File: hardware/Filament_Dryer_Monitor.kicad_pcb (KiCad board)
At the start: 4 copper layers, 91 x 52 mm, 109 parts, among them J1 DC Connector, J2 USB_C_Receptacle_USB2.0_16P, J3 Sensor, J4 Display, J5 Heater Connector, J6 Fan Connector, J7 NTC Connector, Q1 NTD20P06LT4G, Q2 MMBT3904, Q3 MMBT3904, Q4 IRLR3636TRPBF, Q5 IRLML2060TRPBF, Q6 MMBT3904, Q7 MMBT3904, U1 TLV1701, U2 CP2102-GM, U3 AKS1201, U4 ESP32-WROOM-32E-N4, U5 L7987L

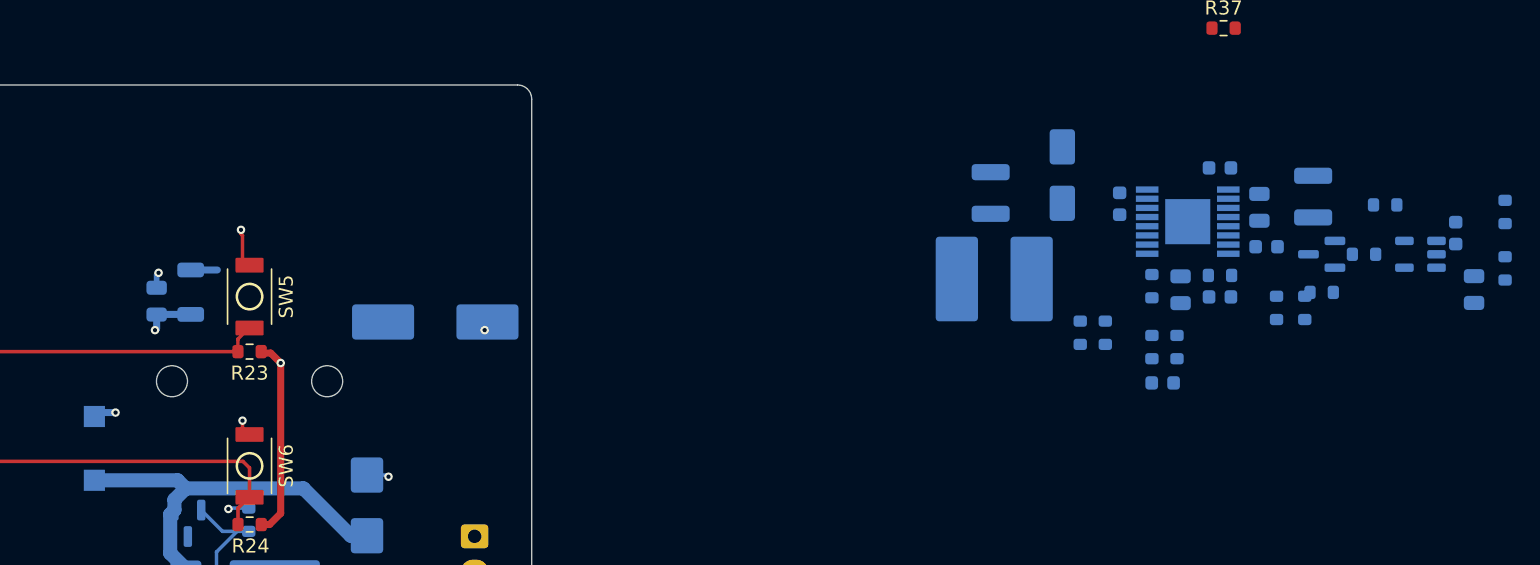
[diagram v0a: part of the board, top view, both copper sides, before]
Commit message: Uopdated buck layout
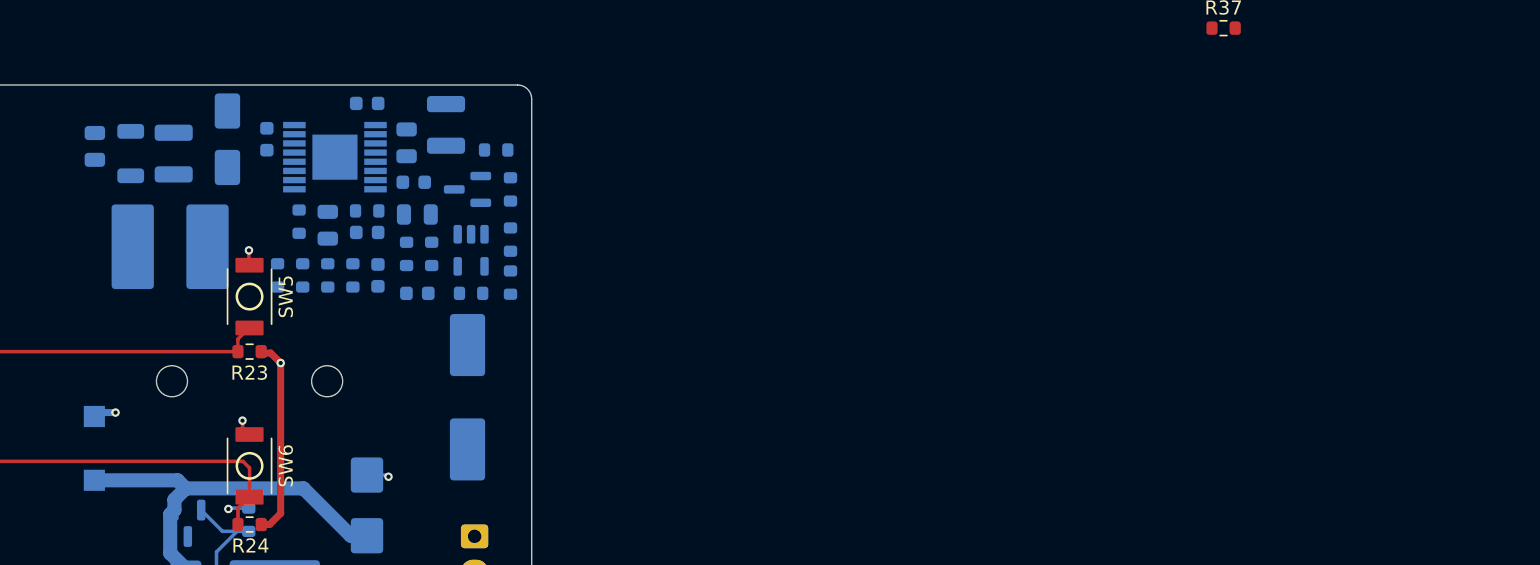
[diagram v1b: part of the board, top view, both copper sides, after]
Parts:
- moved C7 75.1 mm to (182.9, 89.2), turned to 180 degrees
- moved C2 73.7 mm to (182.9, 94.8), turned to 180 degrees
- moved R2 73.3 mm to (186.7, 94.8), turned to 180 degrees
- moved R1 70.7 mm to (189.5, 94.0), turned to -90 degrees
- moved U1 67.3 mm to (186.7, 91.7), turned to -90 degrees
- moved R5 62.1 mm to (189.5, 91.0), turned to 90 degrees
- moved R32 62.0 mm to (183.9, 92.0), turned to -90 degrees
- moved R31 61.8 mm to (182.1, 92.0)
- moved C1 61.7 mm to (184.9, 82.8)
- moved Q7 60.7 mm to (186.4, 87.4)
- moved R6 60.7 mm to (189.5, 87.4), turned to 90 degrees
- moved C4 60.6 mm to (182.6, 86.9)
- moved C21 60.6 mm to (179.3, 81.3)
- moved C3 60.6 mm to (182.1, 84.1)
- moved C6 60.6 mm to (172.2, 83.8)
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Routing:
- net GND: track 55.5 -> 51.1 mm, vias 28 -> 26
- net 3V3_MCU: track 51.5 -> 47.9 mm, vias 13 -> 12
- net Net-(D7-K): track 0.00 -> 1.89 mm
- net /Power/3V3_BUCK: track 1.89 -> 0.00 mm

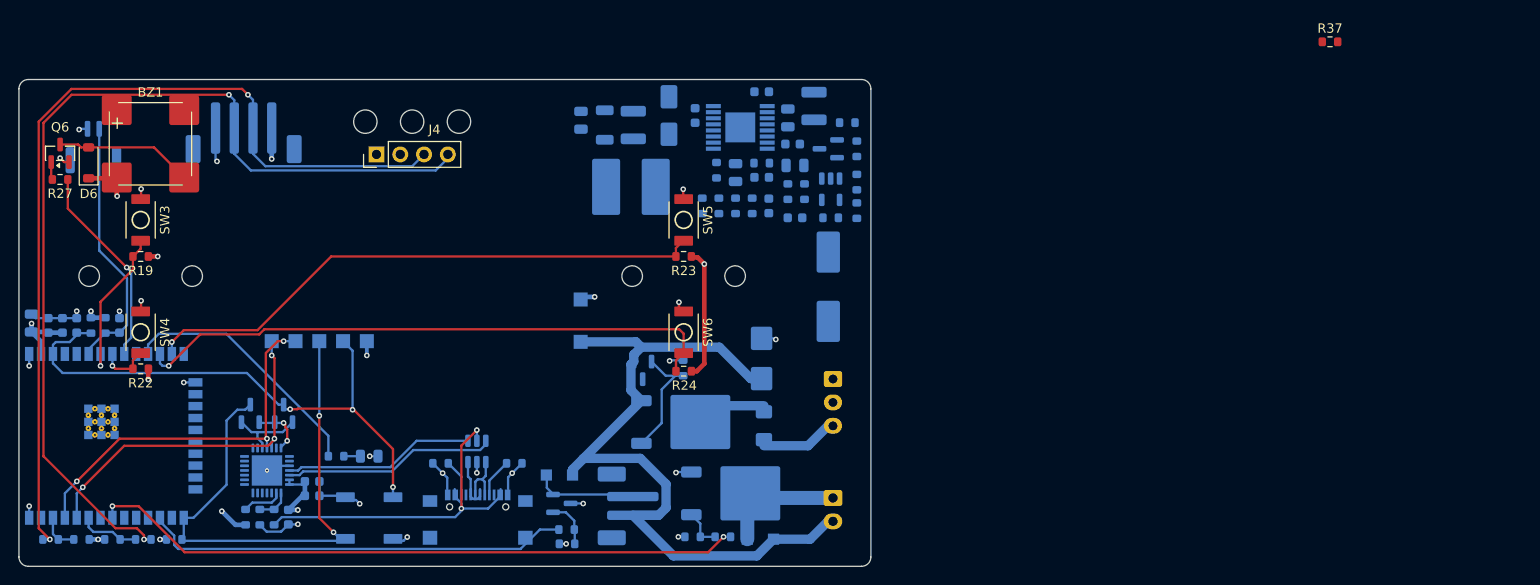
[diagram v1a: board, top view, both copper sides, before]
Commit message: updated layout
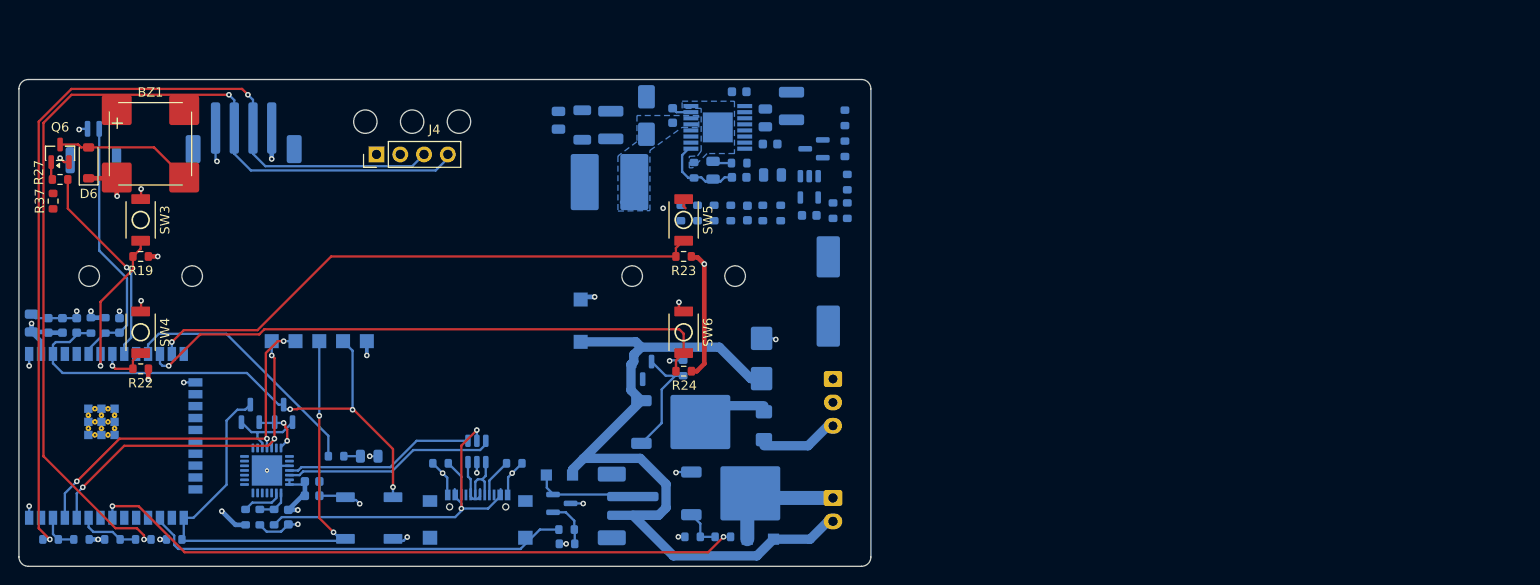
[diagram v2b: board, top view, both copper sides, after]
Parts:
- moved R37 137.5 mm to (103.6, 93.0), turned to 90 degrees
- moved R31 3.52 mm to (179.5, 94.3)
- moved R32 3.42 mm to (181.4, 94.3)
- moved C7 2.61 mm to (180.5, 90.2)
- moved C9 2.42 mm to (174.1, 89.7)
- moved C20 2.41 mm to (177.8, 94.3)
- moved R29 2.41 mm to (170.7, 94.3)
- moved R35 2.41 mm to (176.0, 94.3)
- moved R36 2.41 mm to (174.3, 94.3)
- moved R4 2.41 mm to (172.5, 94.3)
- moved C10 2.40 mm to (163.2, 84.9)
- moved FB1 2.40 mm to (160.2, 84.9)
- moved C1 2.40 mm to (182.5, 82.8)
- moved C11 2.40 mm to (157.6, 84.4)
- moved C21 2.40 mm to (176.9, 81.3)
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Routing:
- net Net-(U5-FB): track 0.00 -> 8.98 mm
- net Net-(U5-BOOT): track 0.00 -> 2.12 mm
- net Net-(C9-Pad1): track 0.00 -> 2.00 mm
- added copper zone on B.Cu, net GND
- added copper zone on B.Cu, net Net-(D7-K)

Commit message: Layout update
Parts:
- turned C1 to 90 degrees
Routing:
- net 3V3_MCU: track 47.9 -> 215.2 mm, vias 12 -> 10
- net 24V_PROT: track 79.7 -> 136.5 mm, vias 0 -> 3
- net /Power/3V3_BUCK: track 0.00 -> 50.3 mm, vias 0 -> 2
- net GND: track 51.1 -> 78.3 mm, vias 26 -> 46
- net /Power/EN: track 0.00 -> 17.6 mm, vias 0 -> 2
- net Net-(D6-A): track 14.7 -> 0.33 mm
- net /Power/COMP: track 0.00 -> 9.65 mm
- net Net-(U5-ILIM): track 0.00 -> 9.01 mm
- net Net-(U5-FSW): track 0.00 -> 8.73 mm
- net /Power/VREF_FAULT: track 0.00 -> 7.88 mm
- net Net-(R5-Pad2): track 0.00 -> 6.15 mm
- net Net-(U5-FB): track 8.98 -> 14.3 mm
- net Net-(Q7-B): track 0.00 -> 4.07 mm
- net Net-(U5-SS): track 0.00 -> 2.27 mm
- net Net-(C20-Pad1): track 0.00 -> 1.80 mm
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- added copper zone on B.Cu, net /Power/3V3_BUCK
- added copper zone on B.Cu, net 24V_PROT
- removed copper zone on In2.Cu, net 3V3_MCU

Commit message: Update Filament_Dryer_Monitor.kicad_pcb
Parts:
- turned D1 to 180 degrees
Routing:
- net GND: track 78.3 -> 83.5 mm, vias 46 -> 47
- net 24V_PROT: track 136.5 -> 139.6 mm

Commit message: Added C22 1uF
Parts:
- moved C5 0.25 mm to (186.2, 102.6)
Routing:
- net 3V3_MCU: track 215.2 -> 231.6 mm
- net Net-(D6-A): track 0.33 -> 9.11 mm
- net 24V_PROT: vias 3 -> 2

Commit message: updated vias on U5 and D7
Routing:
- net GND: vias 47 -> 48
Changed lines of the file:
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@@
+	)
+	(via
+		(at 173.749 87.35)
+		(size 0.6)
+		(drill 0.3)
+		(layers "F.Cu" "B.Cu")
+		(net "GND")
 	)
 	(via
@@
 	(via
 		(at 152.668 129.058)
+		(size 0.6)
+		(drill 0.3)
+		(layers "F.Cu" "B.Cu")
+		(net "GND")
+	)
+	(via
+		(at 173.749 82.9)
 		(size 0.6)
 		(drill 0.3)
@@
 	)
 	(via
+		(at 175.549 82.9)
+		(size 0.6)
+		(drill 0.3)
+		(layers "F.Cu" "B.Cu")
+		(net "GND")
+	)
+	(via
+		(at 175.55 87.35)
+		(size 0.6)
+		(drill 0.3)
+		(layers "F.Cu" "B.Cu")
+		(net "GND")
+	)
+	(via
 		(at 101.092 110.586)
 		(size 0.6)
@@
 	)
 	(via
-		(at 174.649 85.116)
-		(size 0.6)
-		(drill 0.3)
-		(layers "F.Cu" "B.Cu")
-		(net "GND")
-	)
-	(via
-		(at 173.496 86.132)
-		(size 0.6)
-		(drill 0.3)
-		(layers "F.Cu" "B.Cu")
-		(net "GND")
-	)
-	(via
 		(at 170.702 94.335)
 		(size 0.6)
@@
 	)
 	(via
-		(at 175.782 86.132)
-		(size 0.6)
-		(drill 0.3)
-		(layers "F.Cu" "B.Cu")
-		(net "GND")
-	)
-	(via
 		(at 103.646 94.514)
 		(size 0.6)
@@
 	)
 	(via
-		(at 175.782 84.1)
+		(at 174.649 82.9)
+		(size 0.6)
+		(drill 0.3)
+		(layers "F.Cu" "B.Cu")
+		(net "GND")
+	)
+	(via
+		(at 174.65 87.35)
 		(size 0.6)
 		(drill 0.3)
@@
 		(net "GND")
 	)
-	(via
-		(at 173.496 84.1)
-		(size 0.6)
-		(drill 0.3)
-		(layers "F.Cu" "B.Cu")
-		(net "GND")
-	)

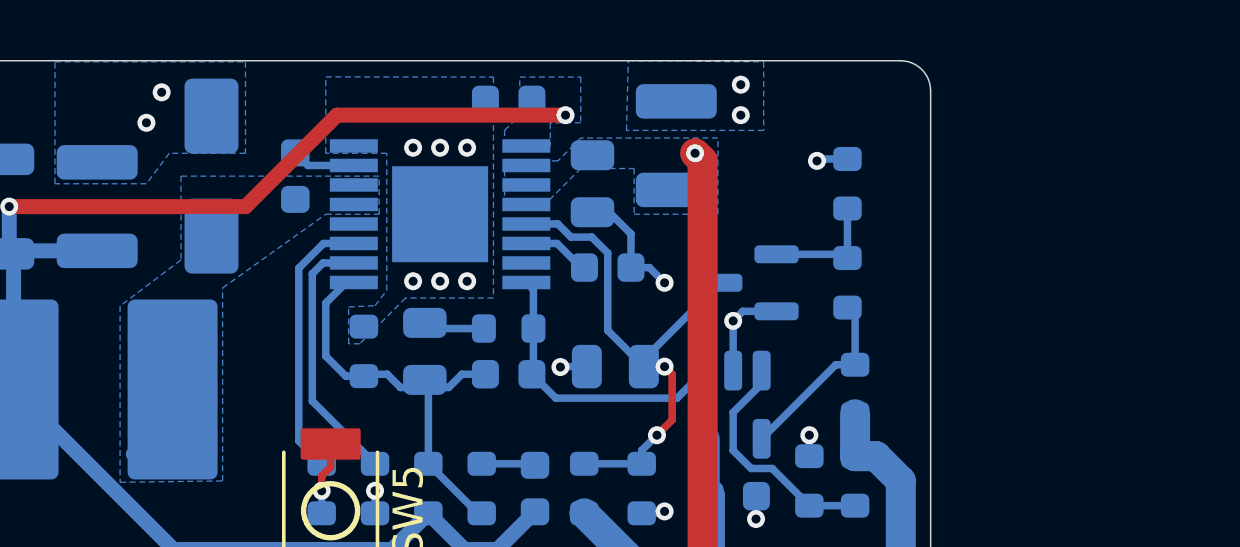
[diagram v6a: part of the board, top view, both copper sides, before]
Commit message: updated D7 footprint
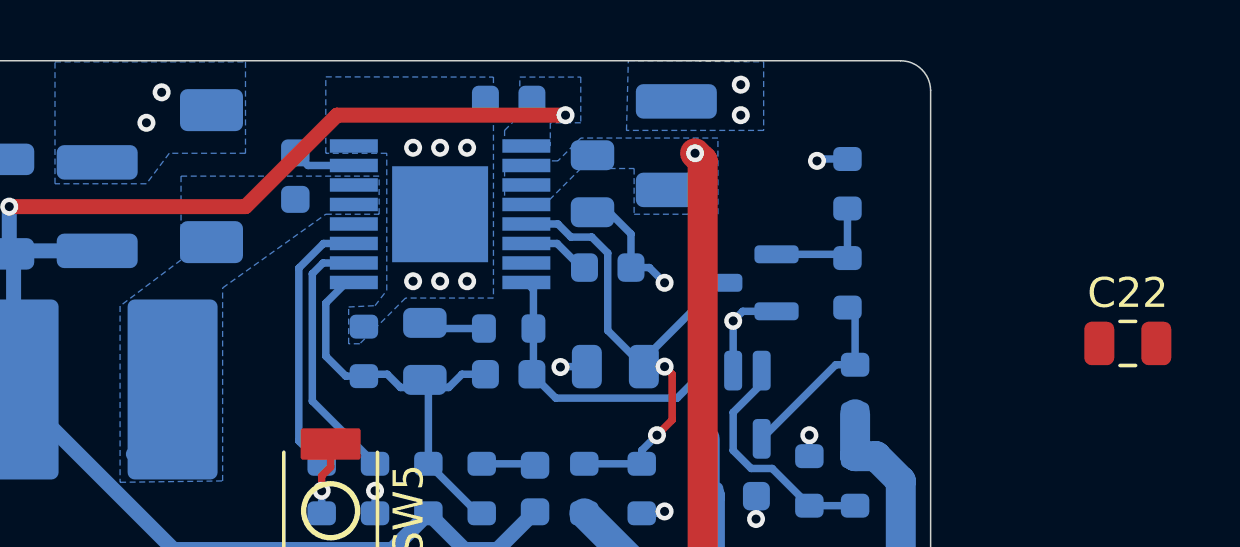
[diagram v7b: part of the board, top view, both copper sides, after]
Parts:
- added C22: 1u, Capacitor_SMD:C_0805_2012Metric, F.Cu at (197.6, 89.4)
- D7: value STPS2L60A -> PMEG6030EP; footprint Diode_SMD:D_SMA -> Diode_SMD:D_SOD-128

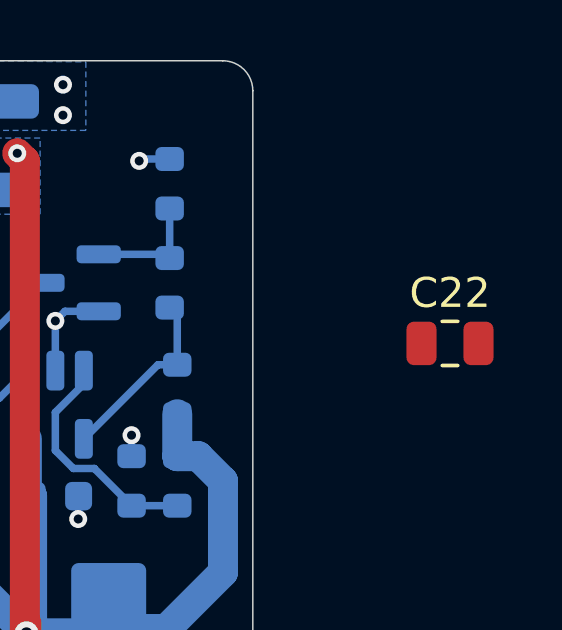
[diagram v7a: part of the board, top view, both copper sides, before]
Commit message: Removed C22
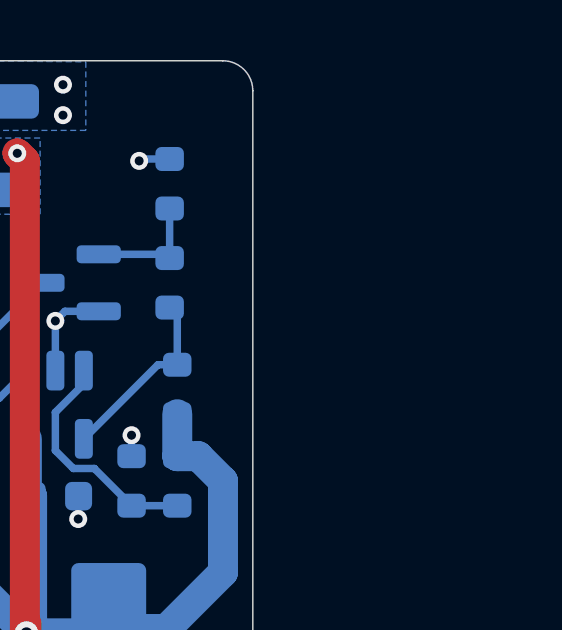
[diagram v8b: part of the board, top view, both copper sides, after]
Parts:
- removed C22: 1u, Capacitor_SMD:C_0805_2012Metric
